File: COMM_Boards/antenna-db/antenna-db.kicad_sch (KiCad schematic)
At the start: 25 parts, among them J1 PC104_Connector

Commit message: COMM: antt-dbd: include disarming pin for testing
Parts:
- removed Q? (x2): BC817W, Package_TO_SOT_SMD:SOT-323_SC-70, symbol Transistor_BJT:BC817W
- removed TP? (x8): TestPoint, symbol Connector:TestPoint
- added J?: Conn_01x02_Male, symbol Connector:Conn_01x02_Male
- added Q? (x2): Q_NPN_Darlington_BCE, symbol Device:Q_NPN_Darlington_BCE
- added R?: 100k, symbol Device:R
- added TP? (x4): TestPoint, symbol Connector:TestPoint
- J1: footprint pc104-connector:pc104-connector -> pc104-template:pc104-connector
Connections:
- net GND: now also R?.2, U?.1 (ADJ), J?.2 (Pin_2), Q?.3 (E), Q?.3 (E)
- net at R?.1, U?.2 (VOUT): now also Q?.3 (C)
- net at R?.2: now also Q?.1 (B) (x2)
- removed net From-Regulator: Q?.3 (C), R?.2, U?.1 (ADJ)
- net Power-Enable renamed POWER_EN
- net POWER_EN: now also R?.1; no longer R?.1
- net To-Resistor: no longer names the net of Q?.2 (E)
- net To-Resistor: now also TP?.1, TP?.1
- new net: Q?.2 (C), TP?.1 (x2)
- new net POWER_EN_R: J?.1 (Pin_1), R?.1, R?.2
- no-connect marks 104 -> 102
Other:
- note added: "ARM ENABLE CONTROL"
- note removed: "Test Points That Connect to 146 MHz Burn Wires"
- note removed: "Test Points That Connect to 436 MHz Burn Wires"
- moved on the sheet: C?, Q?, R?, U?

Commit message: COMM: antt-dbd: map mounting holes to pcb layout
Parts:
- gave numbers to parts that had none: 18
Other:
- removed sheet Temperature Sensor

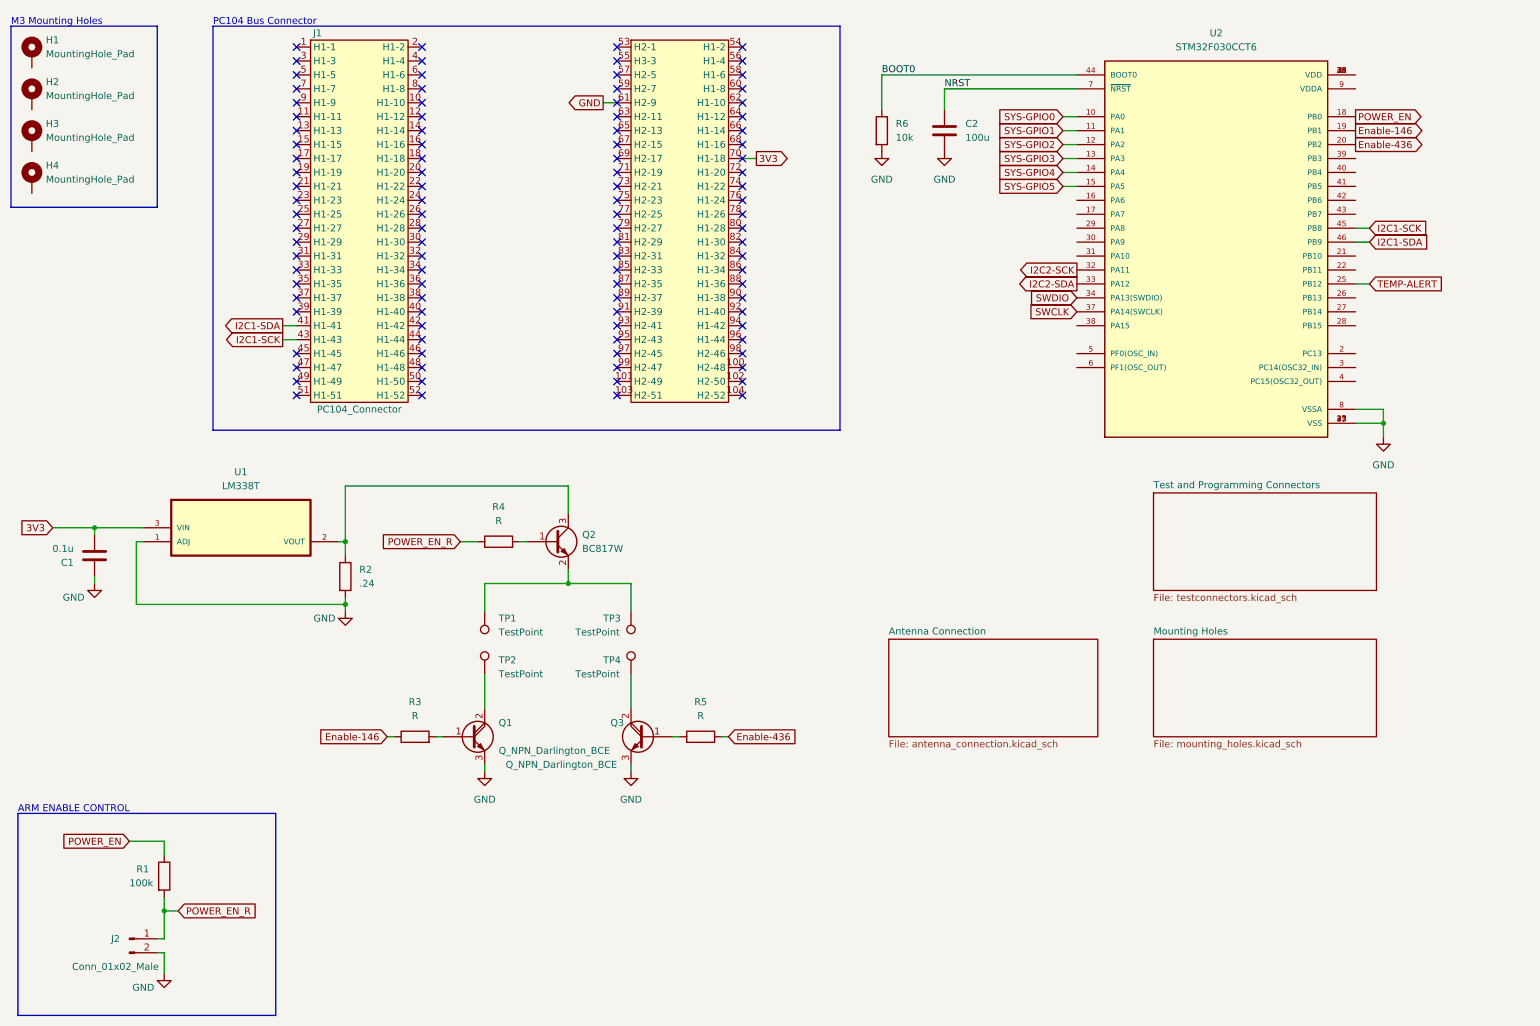
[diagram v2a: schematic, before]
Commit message: include SC4216 regulator
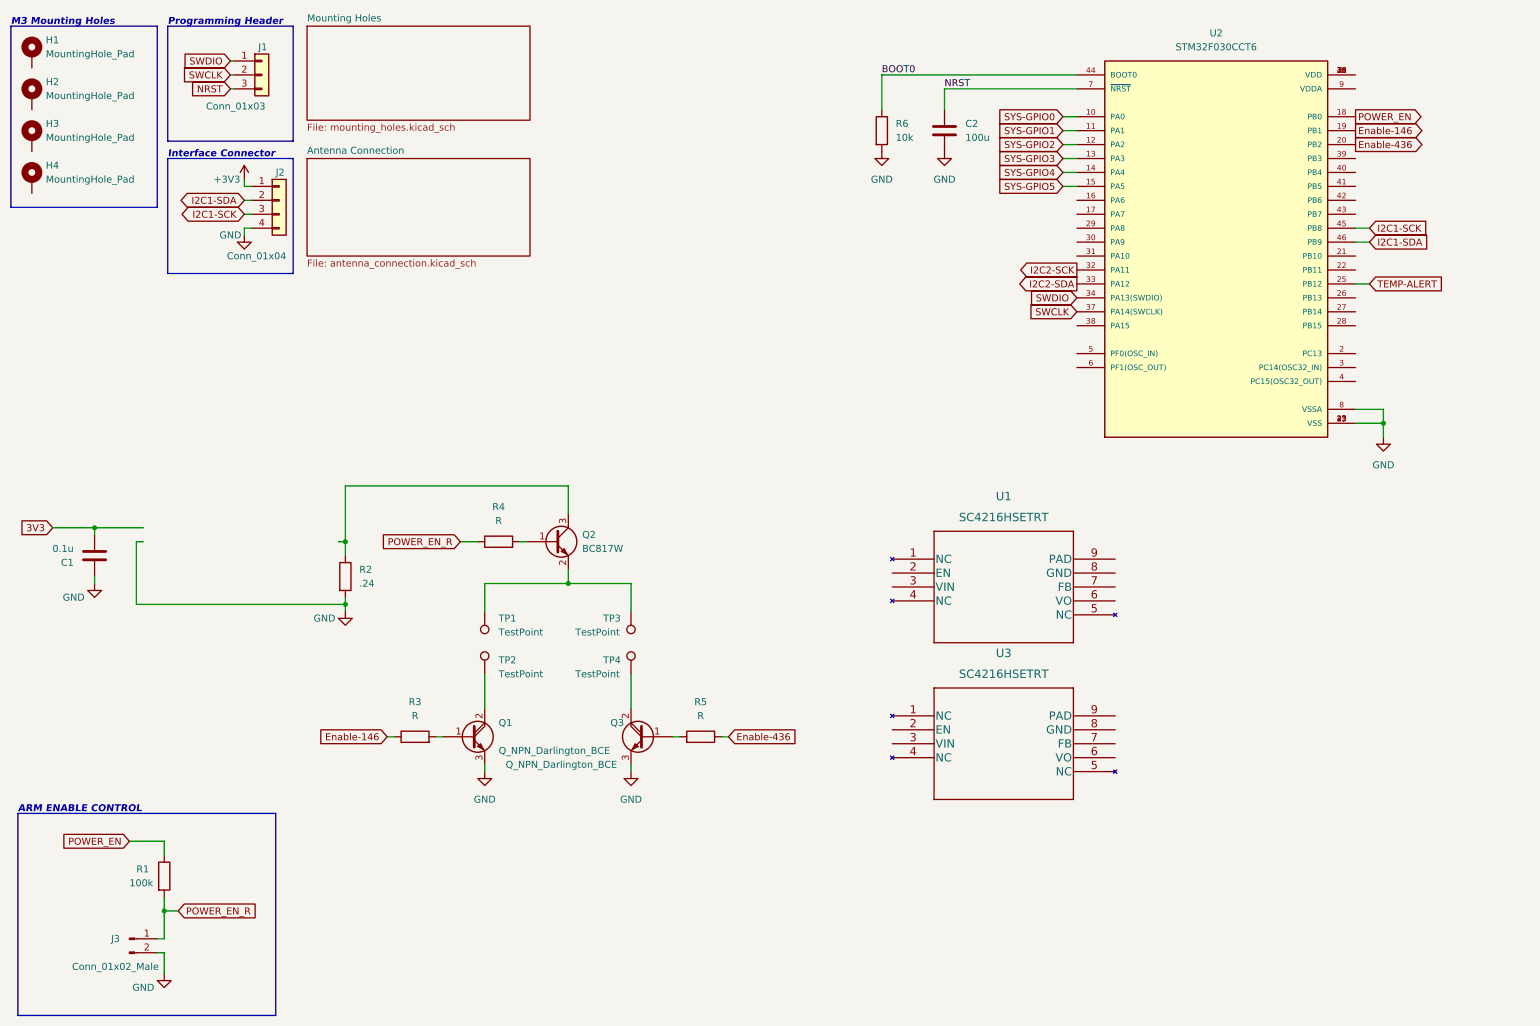
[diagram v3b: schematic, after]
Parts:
- removed J1: PC104_Connector, pc104-template:pc104-connector, symbol qset-connector-library:PC104_Connector
- removed U1: LM338T, TO254P1054X470X1955-3, symbol LM338T:LM338T
- added J1: Conn_01x03, Connector_PinHeader_2.54mm:PinHeader_1x03_P2.54mm_Horizontal, symbol Connector_Generic:Conn_01x03
- added J2: Conn_01x04, Connector_PinHeader_2.54mm:PinHeader_1x04_P2.54mm_Horizontal, symbol Connector_Generic:Conn_01x04
- added U1, U3: SC4216HSETRT, Package_SO:SOIC-8-1EP_3.9x4.9mm_P1.27mm_EP2.29x3mm, symbol SC4216HSETRT:SC4216HSETRT
- J3: renamed from J2; footprint (none) -> Connector_PinHeader_2.54mm:PinHeader_1x02_P2.54mm_Horizontal
- R1: footprint (none) -> Resistor_SMD:R_0603_1608Metric
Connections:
- net GND: now also J2.4 (Pin_4)
- net I2C1-SCK: now also J2.3 (Pin_3)
- net I2C1-SDA: now also J2.2 (Pin_2)
- net NRST: now also J1.3 (Pin_3)
- net SWCLK: now also J1.2 (Pin_2)
- net SWDIO: now also J1.1 (Pin_1)
- new net +3V3: J2.1 (Pin_1)
- no-connect marks 102 -> 0
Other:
- removed sheet Test and Programming Connectors
- note added: "Interface Connector"
- note added: "Programming Header"
- note removed: "PC104 Bus Connector"

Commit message: COMM: antt-dbd: finish deployment detection and arming control
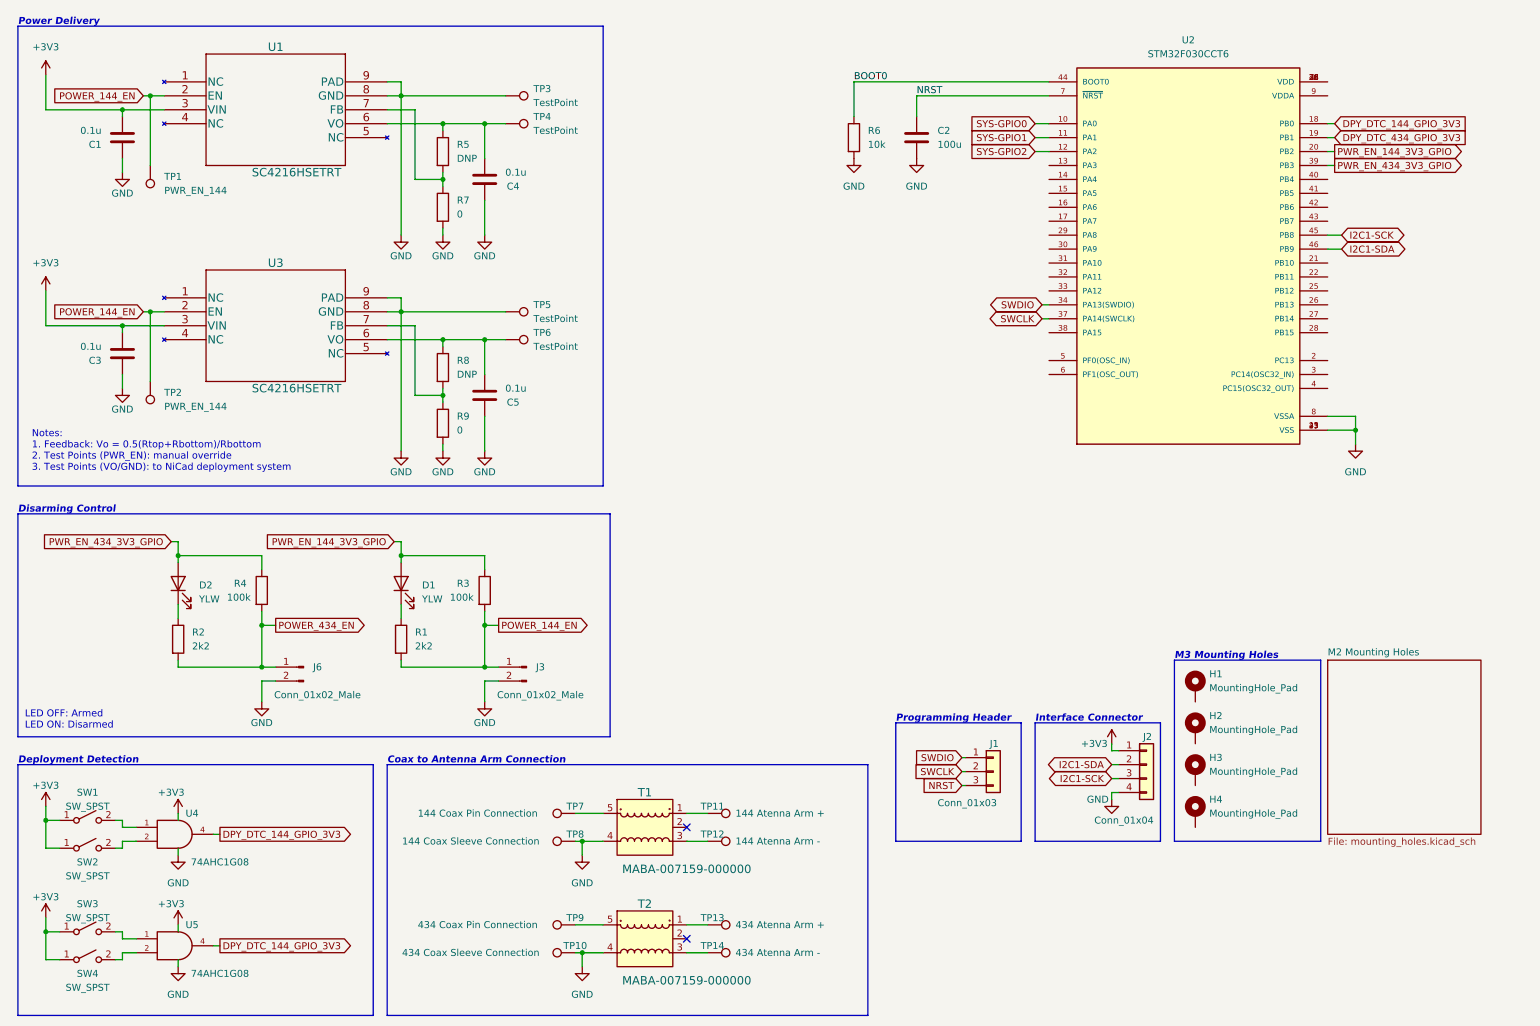
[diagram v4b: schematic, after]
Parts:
- removed Q1, Q3: Q_NPN_Darlington_BCE, symbol Device:Q_NPN_Darlington_BCE
- removed Q2: BC817W, Package_TO_SOT_SMD:SOT-323_SC-70, symbol Transistor_BJT:BC817W
- added C3, C4, C5: 0.1u, Capacitor_SMD:C_0603_1608Metric, symbol Device:C
- added D1, D2: YLW, LED_SMD:LED_0603_1608Metric, symbol Device:LED
- added J6: Conn_01x02_Male, Connector_PinHeader_2.54mm:PinHeader_1x02_P2.54mm_Horizontal, symbol Connector:Conn_01x02_Male
- added R7, R9: 0, Resistor_SMD:R_0603_1608Metric_Pad0.98x0.95mm_HandSolder, symbol Device:R
- added R8: DNP, Resistor_SMD:R_0603_1608Metric_Pad0.98x0.95mm_HandSolder, symbol Device:R
- added SW1, SW2, SW3, SW4: SW_SPST, symbol Switch:SW_SPST
- added T1, T2: MABA-007159-000000, qset-footprints:MABA-007159-000000, symbol dk_Balun:MABA-007159-000000
- added TP10: 434 Coax Sleeve Connection, TestPoint:TestPoint_THTPad_4.0x4.0mm_Drill2.0mm, symbol Connector:TestPoint
- added TP11: 144 Atenna Arm +, TestPoint:TestPoint_THTPad_4.0x4.0mm_Drill2.0mm, symbol Connector:TestPoint
- added TP12: 144 Atenna Arm -, TestPoint:TestPoint_THTPad_4.0x4.0mm_Drill2.0mm, symbol Connector:TestPoint
- added TP13: 434 Atenna Arm +, TestPoint:TestPoint_THTPad_4.0x4.0mm_Drill2.0mm, symbol Connector:TestPoint
- added TP14: 434 Atenna Arm -, TestPoint:TestPoint_THTPad_4.0x4.0mm_Drill2.0mm, symbol Connector:TestPoint
- added TP5, TP6: TestPoint, TestPoint:TestPoint_THTPad_4.0x4.0mm_Drill2.0mm, symbol Connector:TestPoint
- added TP7: 144 Coax Pin Connection, TestPoint:TestPoint_THTPad_4.0x4.0mm_Drill2.0mm, symbol Connector:TestPoint
- added TP8: 144 Coax Sleeve Connection, TestPoint:TestPoint_THTPad_4.0x4.0mm_Drill2.0mm, symbol Connector:TestPoint
- added TP9: 434 Coax Pin Connection, TestPoint:TestPoint_THTPad_4.0x4.0mm_Drill2.0mm, symbol Connector:TestPoint
- added U4, U5: 74AHC1G08, Package_TO_SOT_SMD:SOT-353_SC-70-5, symbol 74xGxx:74AHC1G08
- C1, C2: footprint (none) -> Capacitor_SMD:C_0603_1608Metric
- R1: value 100k -> 2k2
- R2: value .24 -> 2k2; footprint (none) -> Resistor_SMD:R_0603_1608Metric
- R3, R4: value R -> 100k; footprint (none) -> Resistor_SMD:R_0603_1608Metric
- R5: value R -> DNP; footprint (none) -> Resistor_SMD:R_0603_1608Metric_Pad0.98x0.95mm_HandSolder
- R6: footprint (none) -> Resistor_SMD:R_0603_1608Metric
- TP1, TP2: value TestPoint -> PWR_EN_144; footprint (none) -> TestPoint:TestPoint_THTPad_4.0x4.0mm_Drill2.0mm
- TP3, TP4: footprint (none) -> TestPoint:TestPoint_THTPad_4.0x4.0mm_Drill2.0mm
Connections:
- net 3V3 is gone; now on net +3V3: C1.2
- net +3V3: now also U1.3 (VIN), U3.3 (VIN), C3.2, SW1.1 (A), SW2.1 (A), SW3.1 (A), SW4.1 (A), U4.5 (VCC), U5.5 (VCC)
- net GND: now also TP3.1, U1.8 (GND), U1.9 (PAD), U3.8 (GND), U3.9 (PAD), C3.1, C4.1, C5.1, J6.2 (Pin_2), R7.2, R9.2, T1.4, T2.4, TP10.1, TP5.1, TP8.1, U4.3 (GND), U5.3 (GND); no longer R2.2
- net at TP4.1: now also R5.1, U1.6 (VO), C4.2
- net POWER_144_EN: now reaches U3.2 (EN)
- net POWER_144_EN: now also J3.1 (Pin_1), R1.2, R3.2, TP1.1, TP2.1, U1.2 (EN)
- net at U3.6 (VO): now also C5.2, R8.1, TP6.1
- net at U3.7 (FB): now also R8.2, R9.1
- net at R5.2: now also U1.7 (FB), R7.1
- net POWER_434_EN: now reaches R4.2
- net POWER_434_EN: now also R2.2, J6.1 (Pin_1)
- net at R2.1: now also D2.1 (K)
- net PWR_EN_434_3V3_GPIO: now reaches U2.39 (PB3)
- net PWR_EN_434_3V3_GPIO: now also R4.1, D2.2 (A)
- net Enable-146 renamed DPY_DTC_434_GPIO_3V3
- net DPY_DTC_434_GPIO_3V3: no longer R3.1
- net Enable-436 renamed PWR_EN_144_3V3_GPIO
- net PWR_EN_144_3V3_GPIO: now also R3.1, D1.2 (A); no longer R5.1
- net I2C2-SCK: no longer names the net of U2.32 (PA11)
- net I2C2-SDA: no longer names the net of U2.33 (PA12)
- net POWER_EN: no longer names the net of R1.1
- net POWER_EN: now also D1.1 (K); no longer U2.18 (PB0)
- removed net POWER_EN_R: J3.1 (Pin_1), R1.2, R4.1
- net SYS-GPIO3: no longer names the net of U2.13 (PA3)
- net SYS-GPIO4: no longer names the net of U2.14 (PA4)
- net SYS-GPIO5: no longer names the net of U2.15 (PA5)
- net TEMP-ALERT: no longer names the net of U2.25 (PB12)
- new net: T2.3, TP14.1
- new net: T2.5, TP9.1
- new net: SW3.2 (B), U5.1
- new net: T1.5, TP7.1
- new net: T1.3, TP12.1
- new net: T1.1, TP11.1
- new net: SW1.2 (B), U4.1
- new net: SW2.2 (B), U4.2
- new net: T2.1, TP13.1
- new net: SW4.2 (B), U5.2
- new net DPY_DTC_144_GPIO_3V3: U2.18 (PB0), U4.4, U5.4
- no-connect marks 0 -> 2
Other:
- sheet Mounting Holes renamed M2 Mounting Holes
- removed sheet Antenna Connection
- note added: "Coax to Antenna Arm Connection"
- note added: "Deployment Detection"
- note added: "Disarming Control"
- note added: "LED OFF: Armed LED ON: Disarmed"
- note added: "Notes: 1. Feedback: Vo = 0.5(Rtop+Rbottom)/Rbottom 2. Test Points (PWR_EN): manual override 3. Test Points (VO/GND): to NiCad deployment system"
- note added: "Power Delivery"
- note removed: "ARM ENABLE CONTROL"
- company: (none) -> Queen's Space Engineering Team - Satellite
- title: (none) -> Antenna Deployment Board
- moved on the sheet: C2, H1, H2, H3, H4, J1, J2, R6, U2
